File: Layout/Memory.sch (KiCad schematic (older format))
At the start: 1 part

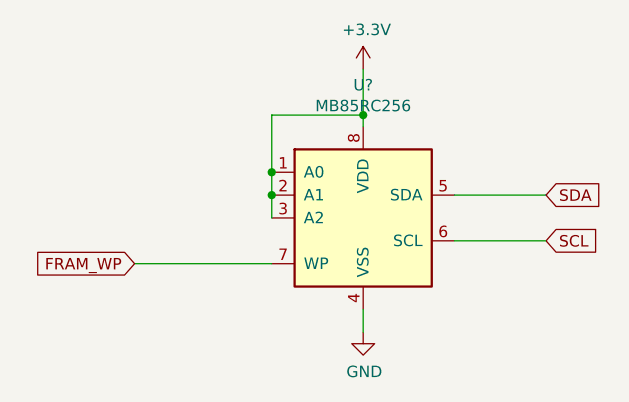
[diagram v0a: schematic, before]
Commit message: Update footprints and references
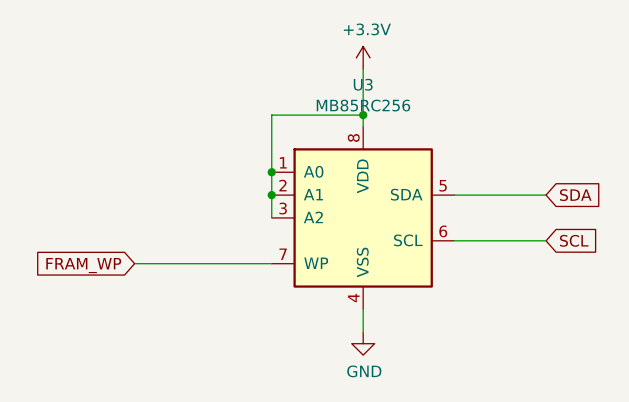
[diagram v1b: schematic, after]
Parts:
- gave numbers to parts that had none: 1
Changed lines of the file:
@@
 $EndDescr
 $Comp
-L Memory_NVRAM:FM24C64B U?
+L Memory_NVRAM:FM24C64B U3
 U 1 1 5F398A90
 P 5550 3550
-F 0 "U?" H 5550 4131 50  0000 C CNN
+F 0 "U3" H 5550 4131 50  0000 C CNN
 F 1 "MB85RC256" H 5550 4040 50  0000 C CNN
 F 2 "Package_SO:SOIC-8_3.9x4.9mm_P1.27mm" H 5550 3550 50  0001 C CNN
@@
 SCL
 $Comp
-L power:GND #PWR?
+L power:GND #PWR0119
 U 1 1 5F3990BA
 P 5550 4050
-F 0 "#PWR?" H 5550 3800 50  0001 C CNN
+F 0 "#PWR0119" H 5550 3800 50  0001 C CNN
 F 1 "GND" H 5555 3877 50  0000 C CNN
 F 2 "" H 5550 4050 50  0001 C CNN
@@
 	5550 4050 5550 3950
 $Comp
-L power:+3.3V #PWR?
+L power:+3.3V #PWR0120
 U 1 1 5F399383
 P 5550 2900
-F 0 "#PWR?" H 5550 2750 50  0001 C CNN
+F 0 "#PWR0120" H 5550 2750 50  0001 C CNN
 F 1 "+3.3V" H 5565 3073 50  0000 C CNN
 F 2 "" H 5550 2900 50  0001 C CNN
